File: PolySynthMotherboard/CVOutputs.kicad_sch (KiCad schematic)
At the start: 117 parts, among them U301 DAC7578xPW, U302 TL074, U303 TL072, U304 TMUX4051, U305 TL074, U306 TMUX4051, U307 TL074, U308 TMUX4051, U309 TMUX4051, U310 TL074, U311 TL074, U312 TL074, U313 TMUX4051, U314 TL074, U315 TL074, U316 TL074, U317 TMUX4051, U318 TMUX4051, U319 TL074, U320 TL072, U321 TL074

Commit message: footprints placed
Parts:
- removed C383, C384: 100n, Capacitor_SMD:C_0805_2012Metric, symbol Device:C
- removed R355, R357: 100k, PCM_Resistor_SMD_AKL:R_0805_2012Metric, symbol Device:R_US
- removed R356, R358: 56k, PCM_Resistor_SMD_AKL:R_0805_2012Metric, symbol Device:R_US
- removed U320: TL072, Package_SO:SOIC-8_3.9x4.9mm_P1.27mm, symbol Amplifier_Operational:TL072
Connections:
- net CUTOFF_DAC: now also U321.14
- net PWM1_DAC: now also U301.5 (VOUTC); no longer U321.14
- net PWM2_DAC: now also U301.12 (VOUTD); no longer U321.8
- net at U321.10 (+): now also U301.7 (VOUTG); no longer U301.12 (VOUTD)
- net at U321.9 (-): now also R301.1, R304.2
- net at U321.12 (+): now also R301.2, U321.8; no longer U301.5 (VOUTC)
- net at U321.13 (-): now also R361.1, R362.2
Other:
- note added: "LVL range: 0-4.191VDC (gain of 1.27)"
- note added: "U321C should give us +/-3v3 per fig. 118 in the datasheet. We want +/-10v so we need a gain of 3.03 from U321D"
- note removed: "LVL range: 0-4.191VDC (gain of 1.27) PWM range: 0-5VDC (gain of 1.5ish)"
- note removed: "U303A should give us +/-3v3 per fig. 118 in the datasheet. We want +/-10v so we need a gain of 3.03 from U303B"
- moved on the sheet: C301, C302, C303, C304, C307, C308, C311, C312, C320, C341, C343, C344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

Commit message: motherboard rev1
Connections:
- net CUTOFF_V1: now also U305.1, U305.2 (-); no longer U305.6 (-), U305.7
- net CUTOFF_V2: now also U310.1, U310.2 (-); no longer U310.6 (-), U310.7
- net CUTOFF_V3: now also U310.13 (-), U310.14; no longer U311.13 (-), U311.14
- net CUTOFF_V4: now also U312.13 (-), U312.14; no longer U314.8, U314.9 (-)
- net CUTOFF_V6: now also U319.6 (-), U319.7; no longer U319.13 (-), U319.14
- net FOLD_V1: now also U305.6 (-), U305.7; no longer U305.1, U305.2 (-)
- net FOLD_V2: now also U310.6 (-), U310.7; no longer U310.1, U310.2 (-)
- net FOLD_V3: now also U310.8, U310.9 (-); no longer U311.8, U311.9 (-)
- net FOLD_V4: now also U312.8, U312.9 (-); no longer U314.6 (-), U314.7
- net FOLD_V5: now also U303.6 (-), U303.7; no longer U316.1, U316.2 (-)
- net LVL1_V3: now also U311.8, U311.9 (-); no longer U310.8, U310.9 (-)
- net LVL1_V4: now also U314.1, U314.2 (-); no longer U312.6 (-), U312.7
- net LVL1_V6: now also U303.1, U303.2 (-); no longer U316.8, U316.9 (-)
- net LVL2_V2: now also U305.8, U305.9 (-); no longer U307.6 (-), U307.7
- net LVL2_V3: now also U311.13 (-), U311.14; no longer U310.13 (-), U310.14
- net LVL2_V4: now also U312.6 (-), U312.7; no longer U312.8, U312.9 (-)
- net LVL2_V6: now also U316.8, U316.9 (-); no longer U316.13 (-), U316.14
- net PWM1_V2: now also U305.13 (-), U305.14; no longer U307.8, U307.9 (-)
- net PWM1_V3: now also U311.6 (-), U311.7; no longer U311.1, U311.2 (-)
- net PWM1_V4: now also U314.8, U314.9 (-); no longer U312.13 (-), U312.14
- net PWM1_V6: now also U316.13 (-), U316.14; no longer U319.1, U319.2 (-)
- net PWM2_V2: now also U307.8, U307.9 (-); no longer U307.13 (-), U307.14
- net PWM2_V3: now also U311.1, U311.2 (-); no longer U311.6 (-), U311.7
- net PWM2_V4: now also U314.13 (-), U314.14; no longer U314.1, U314.2 (-)
- net PWM2_V6: now also U319.13 (-), U319.14; no longer U319.6 (-), U319.7
- net VCA_V1: now also U307.6 (-), U307.7; no longer U305.8, U305.9 (-)
- net VCA_V2: now also U307.13 (-), U307.14; no longer U305.13 (-), U305.14
- net VCA_V4: now also U314.6 (-), U314.7; no longer U314.13 (-), U314.14
- net VCA_V5: now also U316.1, U316.2 (-); no longer U303.1, U303.2 (-)
- net VCA_V6: now also U319.1, U319.2 (-); no longer U303.6 (-), U303.7
- net at C353.1, U313.1 (X4): now also U303.5 (+); no longer U316.3 (+)
- net at C377.1, U318.14 (X1): now also U307.12 (+); no longer U305.12 (+)
- net at C360.1, U317.14 (X1): now also U310.3 (+); no longer U310.5 (+)
- net at C330.1, U308.5 (X5): now also U319.12 (+); no longer U319.5 (+)
- net at C322.1, U306.15 (X2): now also U311.12 (+); no longer U310.12 (+)
- net at C354.1, U313.12 (X3): now also U312.10 (+); no longer U314.5 (+)
- net at C361.1, U317.15 (X2): now also U310.12 (+); no longer U311.12 (+)
- net at C378.1, U318.12 (X3): now also U314.5 (+); no longer U314.12 (+)
- net at C374.1, U318.13 (X0): now also U307.5 (+); no longer U305.10 (+)
- net at C342.1, U309.14 (X1): now also U305.12 (+); no longer U307.10 (+)
- net at C355.1, U313.15 (X2): now also U310.10 (+); no longer U311.10 (+)
- net at C352.1, U313.14 (X1): now also U310.5 (+); no longer U310.3 (+)
- net at C335.1, U308.15 (X2): now also U311.3 (+); no longer U311.5 (+)
- net at C318.1, U304.5 (X5): now also U303.3 (+); no longer U316.10 (+)
- net at C337.1, U308.14 (X1): now also U307.10 (+); no longer U307.12 (+)
- net at C339.1, U309.15 (X2): now also U311.5 (+); no longer U311.3 (+)
- net at C323.1, U306.12 (X3): now also U312.5 (+); no longer U312.10 (+)
- net at C375.1, U318.1 (X4): now also U316.3 (+); no longer U303.3 (+)
- net at C373.1, U318.5 (X5): now also U319.3 (+); no longer U303.5 (+)
- net at C362.1, U317.12 (X3): now also U312.12 (+); no longer U314.10 (+)
- net at C325.1, U306.5 (X5): now also U316.10 (+); no longer U316.12 (+)
- net at C334.1, U309.5 (X5): now also U316.12 (+); no longer U319.3 (+)
- net at C316.1, U304.12 (X3): now also U314.3 (+); no longer U312.5 (+)
- net at C370.1, U317.5 (X5): now also U319.5 (+); no longer U319.12 (+)
- net at C351.1, U313.13 (X0): now also U305.5 (+); no longer U305.3 (+)
- net at C321.1, U306.14 (X1): now also U305.10 (+); no longer U307.5 (+)
- net at C315.1, U304.15 (X2): now also U311.10 (+); no longer U310.10 (+)
- net at C338.1, U309.12 (X3): now also U314.10 (+); no longer U312.12 (+)
- net at C333.1, U308.12 (X3): now also U314.12 (+); no longer U314.3 (+)
- net at C357.1, U317.13 (X0): now also U305.3 (+); no longer U305.5 (+)
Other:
- note added: "The remaining 4 CV signals are designed to work in the 0-3.3V range"
- moved on the sheet: U303A, U303B, U305A, U305B, U305C, U305D, U307B, U307C, U307D, U310A, U310B, U310C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

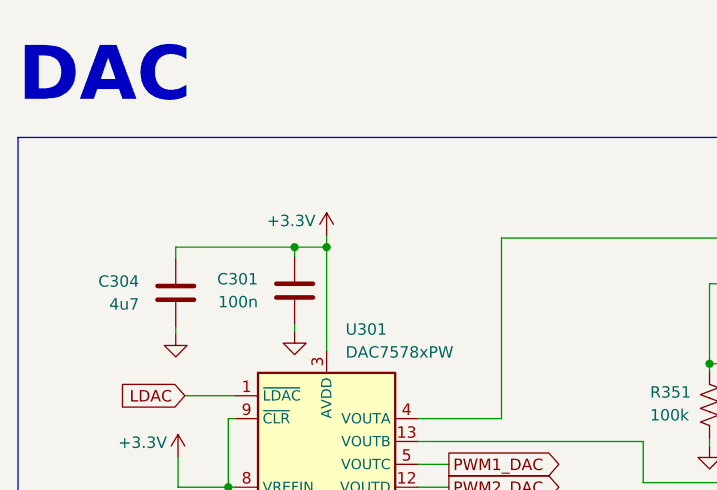
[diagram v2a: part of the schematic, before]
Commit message: updated to kicad 8
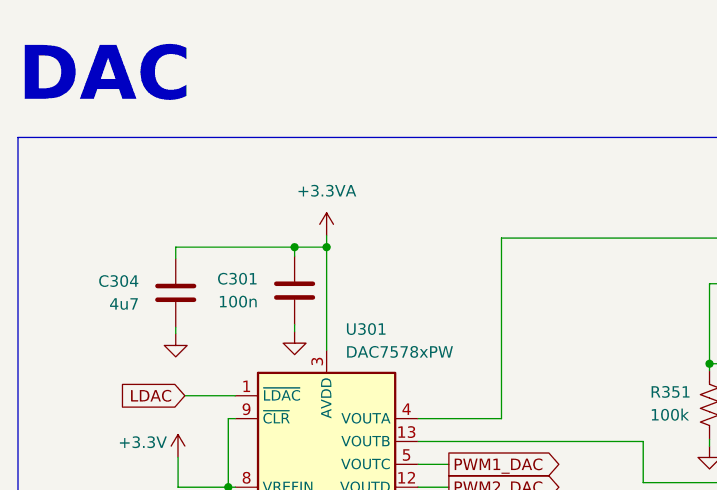
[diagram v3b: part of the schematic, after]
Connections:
- net +3.3V: no longer C301.1, C304.1, U301.3 (AVDD)
- new net +3.3VA: C301.1, C304.1, U301.3 (AVDD)

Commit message: fixed footprints, switched optocoupler
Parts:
- R301, R304, R351, R352, R353, R354, R361, R362: footprint PCM_Resistor_SMD_AKL:R_0805_2012Metric -> Resistor_SMD:R_0805_2012Metric
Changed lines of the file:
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@@
 			)
 		)
-		(property "Footprint" "PCM_Resistor_SMD_AKL:R_0805_2012Metric"
+		(property "Footprint" "Resistor_SMD:R_0805_2012Metric"
 			(at 149.479 55.753 90)
 			(effects
@@
 			)
 		)
-		(property "Footprint" "PCM_Resistor_SMD_AKL:R_0805_2012Metric"
+		(property "Footprint" "Resistor_SMD:R_0805_2012Metric"
 			(at 139.192 61.087 90)
 			(effects
@@
 			)
 		)
-		(property "Footprint" "PCM_Resistor_SMD_AKL:R_0805_2012Metric"
+		(property "Footprint" "Resistor_SMD:R_0805_2012Metric"
 			(at 74.549 129.667 90)
 			(effects
@@
 			)
 		)
-		(property "Footprint" "PCM_Resistor_SMD_AKL:R_0805_2012Metric"
+		(property "Footprint" "Resistor_SMD:R_0805_2012Metric"
 			(at 64.135 136.017 90)
 			(effects
@@
 			)
 		)
-		(property "Footprint" "PCM_Resistor_SMD_AKL:R_0805_2012Metric"
+		(property "Footprint" "Resistor_SMD:R_0805_2012Metric"
 			(at 101.6 54.864 90)
 			(effects
@@
 			)
 		)
-		(property "Footprint" "PCM_Resistor_SMD_AKL:R_0805_2012Metric"
+		(property "Footprint" "Resistor_SMD:R_0805_2012Metric"
 			(at 33.909 127.635 90)
 			(effects
@@
 			)
 		)
-		(property "Footprint" "PCM_Resistor_SMD_AKL:R_0805_2012Metric"
+		(property "Footprint" "Resistor_SMD:R_0805_2012Metric"
 			(at 50.419 127.635 90)
 			(effects
@@
 			)
 		)
-		(property "Footprint" "PCM_Resistor_SMD_AKL:R_0805_2012Metric"
+		(property "Footprint" "Resistor_SMD:R_0805_2012Metric"
 			(at 91.313 60.198 90)
 			(effects

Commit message: board iteration
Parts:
- removed U303: TL072, Package_SO:SOIC-8_3.9x4.9mm_P1.27mm, symbol Amplifier_Operational:TL072
- added C383, C384: 100n, Capacitor_SMD:C_0805_2012Metric, symbol Device:C
- added R302, R303: 12k, Resistor_SMD:R_0805_2012Metric, symbol Device:R_US
- added U303, U320: TL074, Package_SO:SOIC-14_3.9x8.7mm_P1.27mm, symbol Amplifier_Operational:TL074
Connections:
- net +12V: now also C302.1, C383.1, U303.4 (V+), U320.4 (V+); no longer C303.1
- net +3.3V: now also R302.2, R303.2
- net -12V: now also C303.1, C384.1, U303.11 (V-), U320.11 (V-); no longer C302.1
- net CUTOFF_V1: now also U303.6 (-), U303.7; no longer U305.1, U305.2 (-)
- net CUTOFF_V2: now also U307.6 (-), U307.7; no longer U310.1, U310.2 (-)
- net CUTOFF_V3: now also U311.6 (-), U311.7; no longer U310.13 (-), U310.14
- net CUTOFF_V4: now also U314.6 (-), U314.7; no longer U312.13 (-), U312.14
- net CUTOFF_V6: now also U320.6 (-), U320.7; no longer U319.6 (-), U319.7
- net DAC_SCL: now also R302.1
- net DAC_SDA: now also R303.1
- net FOLD_V1: now also U303.8, U303.9 (-); no longer U305.6 (-), U305.7
- net FOLD_V2: now also U307.8, U307.9 (-); no longer U310.6 (-), U310.7
- net FOLD_V3: now also U311.8, U311.9 (-); no longer U310.8, U310.9 (-)
- net FOLD_V4: now also U314.8, U314.9 (-); no longer U312.8, U312.9 (-)
- net FOLD_V5: now also U316.8, U316.9 (-)
- net FOLD_V6: now also U320.8, U320.9 (-); no longer U319.8, U319.9 (-)
- net GND: now also C383.2, C384.2
- net LVL1_V1: now also U302.8, U302.9 (-); no longer U302.6 (-), U302.7
- net LVL1_V2: now also U305.8, U305.9 (-); no longer U307.1, U307.2 (-)
- net LVL1_V3: now also U310.8, U310.9 (-); no longer U311.8, U311.9 (-)
- net LVL1_V4: now also U312.8, U312.9 (-); no longer U314.1, U314.2 (-)
- net LVL1_V5: now also U315.8, U315.9 (-); no longer U315.1, U315.2 (-)
- net LVL1_V6: now also U319.8, U319.9 (-)
- net LVL2_V1: now also U302.6 (-), U302.7; no longer U302.1, U302.2 (-)
- net LVL2_V2: now also U305.6 (-), U305.7; no longer U305.8, U305.9 (-)
- net LVL2_V3: now also U310.6 (-), U310.7; no longer U311.13 (-), U311.14
- net LVL2_V6: now also U319.6 (-), U319.7; no longer U316.8, U316.9 (-)
- net PWM1_V1: now also U302.1, U302.2 (-); no longer U302.8, U302.9 (-)
- net PWM1_V2: now also U305.1, U305.2 (-); no longer U305.13 (-), U305.14
- net PWM1_V3: now also U310.1, U310.2 (-); no longer U311.6 (-), U311.7
- net PWM1_V4: now also U312.1, U312.2 (-); no longer U314.8, U314.9 (-)
- net PWM1_V5: now also U315.1, U315.2 (-); no longer U315.8, U315.9 (-)
- net PWM1_V6: now also U319.1, U319.2 (-); no longer U316.13 (-), U316.14
- net PWM2_V2: now also U305.13 (-), U305.14; no longer U307.8, U307.9 (-)
- net PWM2_V3: now also U310.13 (-), U310.14; no longer U311.1, U311.2 (-)
- net PWM2_V4: now also U312.13 (-), U312.14; no longer U314.13 (-), U314.14
- net VCA_V1: now also U303.1, U303.2 (-); no longer U307.6 (-), U307.7
- net VCA_V2: now also U307.1, U307.2 (-); no longer U307.13 (-), U307.14
- net VCA_V3: now also U311.1, U311.2 (-); no longer U312.1, U312.2 (-)
- net VCA_V4: now also U314.1, U314.2 (-); no longer U314.6 (-), U314.7
- net VCA_V6: now also U320.1, U320.2 (-); no longer U319.1, U319.2 (-)
- net A5_C: now reaches C375.1, U316.3 (+), U318.1 (X4)
- net P1V2_C: now reaches C342.1, U309.14 (X1)
- net P1V2_C: now also U305.3 (+); no longer U305.12 (+)
- net FV2_C: now reaches C352.1, U313.14 (X1)
- net FV2_C: now also U307.10 (+); no longer U310.5 (+)
- net C6_C: now reaches C370.1, U317.5 (X5)
- net C6_C: now also U320.5 (+); no longer U319.5 (+)
- net L1V1_C: now reaches C314.1, U304.13 (X0)
- net L1V1_C: now also U302.10 (+); no longer U302.5 (+)
- net L2V3_C: now reaches C322.1, U306.15 (X2)
- net L2V3_C: now also U310.5 (+); no longer U311.12 (+)
- net C5_C: now reaches C369.1, U316.5 (+), U317.1 (X4)
- net A4_C: now reaches C378.1, U318.12 (X3)
- net A4_C: now also U314.3 (+); no longer U314.5 (+)
- net P2V4_C: now reaches C333.1, U308.12 (X3)
- net P2V4_C: now also U312.12 (+); no longer U314.12 (+)
- net C2_C: now reaches C360.1, U317.14 (X1)
- net C2_C: now also U307.5 (+); no longer U310.3 (+)
- net L2V5_C: now reaches C324.1, U306.1 (X4), U315.5 (+)
- net L1V2_C: now reaches C313.1, U304.14 (X1)
- net L1V2_C: now also U305.10 (+); no longer U307.3 (+)
- net P2V1_C: now reaches C332.1, U302.12 (+), U308.13 (X0)
- net L2V2_C: now reaches C321.1, U306.14 (X1)
- net L2V2_C: now also U305.5 (+); no longer U305.10 (+)
- net P2V2_C: now reaches C337.1, U308.14 (X1)
- net P2V2_C: now also U305.12 (+); no longer U307.10 (+)
- net L1V3_C: now reaches C315.1, U304.15 (X2)
- net L1V3_C: now also U310.10 (+); no longer U311.10 (+)
- net P2V3_C: now reaches C335.1, U308.15 (X2)
- net P2V3_C: now also U310.12 (+); no longer U311.3 (+)
- net L2V6_C: now reaches C325.1, U306.5 (X5)
- net L2V6_C: now also U319.5 (+); no longer U316.10 (+)
- net A2_C: now reaches C377.1, U318.14 (X1)
- net A2_C: now also U307.3 (+); no longer U307.12 (+)
- net C3_C: now reaches C361.1, U317.15 (X2)
- net C3_C: now also U311.5 (+); no longer U310.12 (+)
- net P1V3_C: now reaches C339.1, U309.15 (X2)
- net P1V3_C: now also U310.3 (+); no longer U311.5 (+)
- net P1V1_C: now reaches C340.1, U309.13 (X0)
- net P1V1_C: now also U302.3 (+); no longer U302.10 (+)
- net L1V5_C: now reaches C317.1, U304.1 (X4)
- net L1V5_C: now also U315.10 (+); no longer U315.3 (+)
- net L2V4_C: now reaches C323.1, U306.12 (X3), U312.5 (+)
- net A1_C: now reaches C374.1, U318.13 (X0)
- net A1_C: now also U303.3 (+); no longer U307.5 (+)
- net A3_C: now reaches C376.1, U318.15 (X2)
- net A3_C: now also U311.3 (+); no longer U312.3 (+)
- net A6_C: now reaches C373.1, U318.5 (X5)
- net A6_C: now also U320.3 (+); no longer U319.3 (+)
- net P2V6_C: now reaches C330.1, U308.5 (X5), U319.12 (+)
- net P1V4_C: now reaches C338.1, U309.12 (X3)
- net P1V4_C: now also U312.3 (+); no longer U314.10 (+)
- net P1V6_C: now reaches C334.1, U309.5 (X5)
- net P1V6_C: now also U319.3 (+); no longer U316.12 (+)
- net FV4_C: now reaches C354.1, U313.12 (X3)
- net FV4_C: now also U314.10 (+); no longer U312.10 (+)
- net FV1_C: now reaches C351.1, U313.13 (X0)
- net FV1_C: now also U303.10 (+); no longer U305.5 (+)
- net L2V1_C: now reaches C319.1, U306.13 (X0)
- net L2V1_C: now also U302.5 (+); no longer U302.3 (+)
- net FV5_C: now reaches C353.1, U313.1 (X4)
- net FV5_C: now also U316.10 (+)
- net FV3_C: now reaches C355.1, U313.15 (X2)
- net FV3_C: now also U311.10 (+); no longer U310.10 (+)
- net FV6_C: now reaches C356.1, U313.5 (X5)
- net FV6_C: now also U320.10 (+); no longer U319.10 (+)
- net L1V6_C: now reaches C318.1, U304.5 (X5)
- net L1V6_C: now also U319.10 (+)
- net L1V4_C: now reaches C316.1, U304.12 (X3)
- net L1V4_C: now also U312.10 (+); no longer U314.3 (+)
- net P1V5_C: now reaches C336.1, U309.1 (X4)
- net P1V5_C: now also U315.3 (+); no longer U315.10 (+)
- net C4_C: now reaches C362.1, U317.12 (X3)
- net C4_C: now also U314.5 (+); no longer U312.12 (+)
- net P2V5_C: now reaches C331.1, U308.1 (X4), U315.12 (+)
- net C1_C: now reaches C357.1, U317.13 (X0)
- net C1_C: now also U303.5 (+); no longer U305.3 (+)
- net DAC_A0 renamed MUX_A0
- net DAC_A1 renamed MUX_A1
- net DAC_A2 renamed MUX_A2
- net DAC_INH renamed MUX_INH
- no-connect marks 15 -> 33
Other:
- note added: "Power pins and extra units"
- note removed: "Power Pins"
- moved on the sheet: C301, C304, C305, C306, C309, C310, C313, C314, C315, C316, C317, C318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

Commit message: larger board routed
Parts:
- removed U303, U307, U311, U314, U316, U320: TL074, Package_SO:SOIC-14_3.9x8.7mm_P1.27mm, symbol Amplifier_Operational:TL074
- added C385, C386, C387, C388: 100n, Capacitor_SMD:C_0805_2012Metric, symbol Device:C
- added U303, U307, U311, U314, U316, U320, U323: TL072, Package_SO:SOIC-8_3.9x4.9mm_P1.27mm, symbol Amplifier_Operational:TL072
- added U322: TL074, Package_SO:SOIC-14_3.9x8.7mm_P1.27mm, symbol Amplifier_Operational:TL074
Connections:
- net +3.3VA is gone; now on net +3.3V: C301.1, C304.1, U301.3 (AVDD)
- net +12V: now also C385.1, C387.1, U303.8 (V+), U307.8 (V+), U311.8 (V+), U314.8 (V+), U316.8 (V+), U320.8 (V+), U322.4 (V+), U323.8 (V+)
- net -12V: now also C371.2, C386.1, C388.1, U303.4 (V-), U307.4 (V-), U311.4 (V-), U314.4 (V-), U316.4 (V-), U320.4 (V-), U322.11 (V-), U323.4 (V-); no longer C371.1
- net A1_C: now also U322.12 (+)
- net A2_C: now also U322.3 (+)
- net A3_C: now also U322.5 (+)
- net A4_C: now also U322.10 (+)
- net A5_C: now also U323.5 (+)
- net A6_C: now also U323.3 (+)
- net C1_C: now also U319.12 (+)
- net C2_C: now also U319.3 (+)
- net C3_C: now also U319.5 (+)
- net C4_C: now also U319.10 (+)
- net C5_C: now also U320.5 (+)
- net C6_C: now also U320.3 (+)
- net CUTOFF_V1: now also U319.13 (-), U319.14
- net CUTOFF_V2: now also U319.1, U319.2 (-)
- net CUTOFF_V3: now also U319.6 (-), U319.7
- net CUTOFF_V4: now also U319.8, U319.9 (-)
- net CUTOFF_V5: now also U320.6 (-), U320.7
- net CUTOFF_V6: now also U320.1, U320.2 (-)
- net FOLD_V1: now also U315.13 (-), U315.14
- net FOLD_V2: now also U315.1, U315.2 (-)
- net FOLD_V3: now also U315.6 (-), U315.7
- net FOLD_V4: now also U315.8, U315.9 (-)
- net FOLD_V5: now also U316.6 (-), U316.7
- net FOLD_V6: now also U316.1, U316.2 (-)
- net FV1_C: now also U315.12 (+)
- net FV2_C: now also U315.3 (+)
- net FV3_C: now also U315.5 (+)
- net FV4_C: now also U315.10 (+)
- net FV5_C: now also U316.5 (+)
- net FV6_C: now also U316.3 (+)
- net GND: now also C371.1, C385.2, C386.2, C387.2, C388.2; no longer C371.2
- net L1V1_C: now also U302.12 (+); no longer U302.10 (+)
- net L1V2_C: now also U302.3 (+); no longer U305.10 (+)
- net L1V3_C: now also U302.5 (+); no longer U310.10 (+)
- net L1V4_C: now also U302.10 (+); no longer U312.10 (+)
- net L1V5_C: now also U303.5 (+); no longer U315.10 (+)
- net L1V6_C: now also U303.3 (+); no longer U319.10 (+)
- net L2V1_C: now also U305.12 (+); no longer U302.5 (+)
- net L2V2_C: now also U305.3 (+); no longer U305.5 (+)
- net L2V3_C: now also U305.5 (+); no longer U310.5 (+)
- net L2V4_C: now also U305.10 (+); no longer U312.5 (+)
- net L2V5_C: now also U307.5 (+); no longer U315.5 (+)
- net L2V6_C: now also U307.3 (+); no longer U319.5 (+)
- net LVL1_V1: now also U302.13 (-), U302.14; no longer U302.8, U302.9 (-)
- net LVL1_V2: now also U302.1, U302.2 (-); no longer U305.8, U305.9 (-)
- net LVL1_V3: now also U302.6 (-), U302.7; no longer U310.8, U310.9 (-)
- net LVL1_V4: now also U302.8, U302.9 (-); no longer U312.8, U312.9 (-)
- net LVL1_V5: now also U303.6 (-), U303.7; no longer U315.8, U315.9 (-)
- net LVL1_V6: now also U303.1, U303.2 (-); no longer U319.8, U319.9 (-)
- net LVL2_V1: now also U305.13 (-), U305.14; no longer U302.6 (-), U302.7
- net LVL2_V2: now also U305.1, U305.2 (-); no longer U305.6 (-), U305.7
- net LVL2_V3: now also U305.6 (-), U305.7; no longer U310.6 (-), U310.7
- net LVL2_V4: now also U305.8, U305.9 (-); no longer U312.6 (-), U312.7
- net LVL2_V5: now also U307.6 (-), U307.7; no longer U315.6 (-), U315.7
- net LVL2_V6: now also U307.1, U307.2 (-); no longer U319.6 (-), U319.7
- net P1V1_C: now also U310.12 (+); no longer U302.3 (+)
- net P1V2_C: now also U310.3 (+); no longer U305.3 (+)
- net P1V3_C: now also U310.5 (+); no longer U310.3 (+)
- net P1V4_C: now also U310.10 (+); no longer U312.3 (+)
- net P1V5_C: now also U311.5 (+); no longer U315.3 (+)
- net P1V6_C: now also U311.3 (+); no longer U319.3 (+)
- net P2V1_C: now also U312.12 (+); no longer U302.12 (+)
- net P2V2_C: now also U312.3 (+); no longer U305.12 (+)
- net P2V3_C: now also U312.5 (+); no longer U310.12 (+)
- net P2V4_C: now also U312.10 (+); no longer U312.12 (+)
- net P2V5_C: now also U314.5 (+); no longer U315.12 (+)
- net P2V6_C: now also U314.3 (+); no longer U319.12 (+)
- net PWM1_V1: now also U310.13 (-), U310.14; no longer U302.1, U302.2 (-)
- net PWM1_V2: now also U310.1, U310.2 (-); no longer U305.1, U305.2 (-)
- net PWM1_V3: now also U310.6 (-), U310.7; no longer U310.1, U310.2 (-)
- net PWM1_V4: now also U310.8, U310.9 (-); no longer U312.1, U312.2 (-)
- net PWM1_V5: now also U311.6 (-), U311.7; no longer U315.1, U315.2 (-)
- net PWM1_V6: now also U311.1, U311.2 (-); no longer U319.1, U319.2 (-)
- net PWM2_V1: now also U312.13 (-), U312.14; no longer U302.13 (-), U302.14
- net PWM2_V2: now also U312.1, U312.2 (-); no longer U305.13 (-), U305.14
- net PWM2_V3: now also U312.6 (-), U312.7; no longer U310.13 (-), U310.14
- net PWM2_V4: now also U312.8, U312.9 (-); no longer U312.13 (-), U312.14
- net PWM2_V5: now also U314.6 (-), U314.7; no longer U315.13 (-), U315.14
- net PWM2_V6: now also U314.1, U314.2 (-); no longer U319.13 (-), U319.14
- net VCA_V1: now also U322.13 (-), U322.14
- net VCA_V2: now also U322.1, U322.2 (-)
- net VCA_V3: now also U322.6 (-), U322.7
- net VCA_V4: now also U322.8, U322.9 (-)
- net VCA_V5: now also U323.6 (-), U323.7
- net VCA_V6: now also U323.1, U323.2 (-)
- no-connect marks 33 -> 15
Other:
- note removed: "Power pins and extra units"
- moved on the sheet: C301, C304, C313, C320, C341, C349, C357, C358, C359, C360, C361, C362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
